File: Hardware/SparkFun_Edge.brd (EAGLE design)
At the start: 40 x 40 mm, 95 parts, among them J5 CORTEX_DEBUG, J7 CAMERA-HIMAX, U2 LIS2DH12, U3 1.8V, U5 ARTEMIS_MODULESMD, Y2 32.768kHz

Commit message: Rename files. Remove dependancy on Ambiq lbr. Remove ambiq.lbr.
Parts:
- C1, C10, C18, C20, C22, C9: device ambiq:0402-TIGHT -> SparkFun-Capacitors:0402-TIGHT
- C23: value 1.0uF -> 0.1uF; device ambiq:0402-TIGHT -> SparkFun-Capacitors:0402-TIGHT
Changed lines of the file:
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@@
 <?xml version="1.0" encoding="utf-8"?>
 <!DOCTYPE eagle SYSTEM "eagle.dtd">
-<eagle version="9.5.1">
+<eagle version="9.4.2">
 <drawing>
 <settings>
@@
 <attribute name="VALUE" x="26.0134" y="16.9958" size="0.6096" layer="27" font="vector" ratio="20" rot="R90" align="top-center"/>
 </element>
-<element name="C9" library="ambiq" package="0402-TIGHT" value="15pF" x="23" y="16" smashed="yes" rot="R270">
+<element name="C9" library="SparkFun-Capacitors" package="0402-TIGHT" value="15pF" x="23" y="16" smashed="yes" rot="R270">
 <attribute name="NAME" x="23.562" y="16" size="0.6096" layer="25" font="vector" ratio="20" rot="R270" align="bottom-center"/>
 <attribute name="PROD_ID" value="CAP-13063" x="23" y="16" size="1.778" layer="27" font="vector" ratio="15" rot="R270" display="off"/>
 <attribute name="VALUE" x="22.438" y="15.746" size="0.6096" layer="27" font="vector" ratio="20" rot="R270" align="top-center"/>
 </element>
-<element name="C10" library="ambiq" package="0402-TIGHT" value="15pF" x="23" y="18" smashed="yes" rot="R90">
+<element name="C10" library="SparkFun-Capacitors" package="0402-TIGHT" value="15pF" x="23" y="18" smashed="yes" rot="R90">
 <attribute name="NAME" x="22.438" y="18" size="0.6096" layer="25" font="vector" ratio="20" rot="R90" align="bottom-center"/>
 <attribute name="PROD_ID" value="CAP-13063" x="23" y="18" size="1.778" layer="27" font="vector" ratio="15" rot="R90" display="off"/>
@@
 <attribute name="VALUE" x="24.5902" y="10.9964" size="0.6096" layer="27" font="vector" ratio="20" rot="R90" align="top-center"/>
 </element>
-<element name="C20" library="ambiq" package="0402-TIGHT" value="0.1uF" x="22.5" y="11" smashed="yes" rot="R270">
+<element name="C20" library="SparkFun-Capacitors" package="0402-TIGHT" value="0.1uF" x="22.5" y="11" smashed="yes" rot="R270">
 <attribute name="NAME" x="23.062" y="11" size="0.6096" layer="25" font="vector" ratio="20" rot="R270" align="bottom-center"/>
 <attribute name="PROD_ID" value="CAP-12416" x="22.5" y="11" size="1.778" layer="27" font="vector" ratio="15" rot="R270" display="off"/>
@@
 <attribute name="VALUE" x="18.408" y="28.734" size="0.4064" layer="27"/>
 </element>
-<element name="C22" library="ambiq" package="0402-TIGHT" value="1.0uF" x="21" y="29" smashed="yes" rot="R270">
+<element name="C22" library="SparkFun-Capacitors" package="0402-TIGHT" value="1.0uF" x="21" y="29" smashed="yes" rot="R270">
 <attribute name="NAME" x="21.562" y="29" size="0.6096" layer="25" font="vector" ratio="20" rot="R270" align="bottom-center"/>
 <attribute name="PROD_ID" value="CAP-12417" x="21" y="29" size="1.778" layer="27" font="vector" ratio="15" rot="R270" display="off"/>
 <attribute name="VALUE" x="20.575" y="30.147" size="0.6096" layer="27" font="vector" ratio="20" rot="R270" align="top-center"/>
 </element>
-<element name="C23" library="ambiq" package="0402-TIGHT" value="1.0uF" x="19" y="31.5" smashed="yes">
+<element name="C23" library="SparkFun-Capacitors" package="0402-TIGHT" value="0.1uF" x="19" y="31.5" smashed="yes">
 <attribute name="NAME" x="19" y="32.062" size="0.6096" layer="25" font="vector" ratio="20" align="bottom-center"/>
-<attribute name="PROD_ID" value="CAP-12417" x="19" y="31.5" size="1.778" layer="27" font="vector" ratio="15" display="off"/>
-<attribute name="VALUE" x="19" y="30.938" size="0.6096" layer="27" font="vector" ratio="20" align="top-center"/>
+<attribute name="PROD_ID" value="CAP-12416" x="19" y="31.5" size="1.778" layer="27" font="vector" ratio="15" display="off"/>
+<attribute name="VALUE" value="0.1uF" x="19" y="30.938" size="0.6096" layer="27" font="vector" ratio="20" align="top-center"/>
 </element>
 <element name="D4" library="SparkFun-LED" package="LED-0603" value="BLUE" x="17" y="4" smashed="yes" rot="R270">
@@
 <attribute name="VALUE" x="11" y="20.762" size="0.6096" layer="27" font="vector" ratio="20" rot="R180" align="top-center"/>
 </element>
-<element name="C18" library="ambiq" package="0402-TIGHT" value="0.1uF" x="5.5" y="30" smashed="yes" rot="R90">
+<element name="C18" library="SparkFun-Capacitors" package="0402-TIGHT" value="0.1uF" x="5.5" y="30" smashed="yes" rot="R90">
 <attribute name="NAME" x="4.938" y="30" size="0.6096" layer="25" font="vector" ratio="20" rot="R90" align="bottom-center"/>
 <attribute name="PROD_ID" value="CAP-12416" x="5.5" y="30" size="1.778" layer="27" font="vector" ratio="15" rot="R90" display="off"/>
@@
 <attribute name="VALUE" x="0.1" y="11.6" size="0.6" layer="27" font="vector" rot="R270"/>
 </element>
-<element name="C1" library="ambiq" package="0402-TIGHT" value="0.1uF" x="5.5" y="10" smashed="yes" rot="R90">
+<element name="C1" library="SparkFun-Capacitors" package="0402-TIGHT" value="0.1uF" x="5.5" y="10" smashed="yes" rot="R90">
 <attribute name="NAME" x="4.938" y="10" size="0.6096" layer="25" font="vector" ratio="20" rot="R90" align="bottom-center"/>
 <attribute name="PROD_ID" value="CAP-12416" x="-0.5" y="6" size="1.778" layer="27" font="vector" ratio="15" rot="R90" display="off"/>

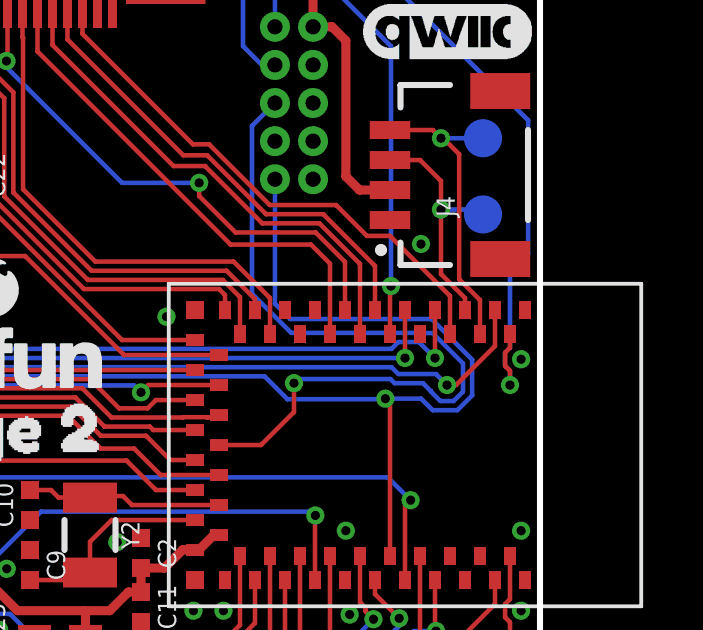
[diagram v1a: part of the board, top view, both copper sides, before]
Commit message: add gpio numbers to camera nets for ease of use
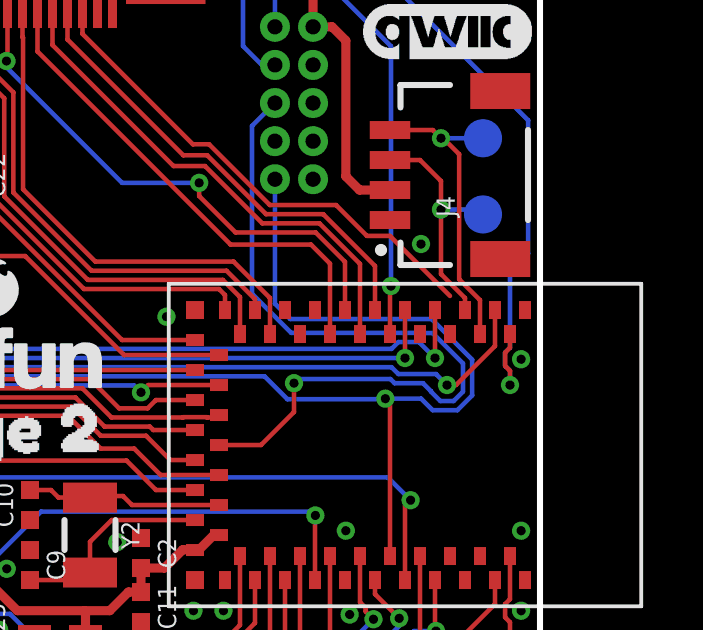
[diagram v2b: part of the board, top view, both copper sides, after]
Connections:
- net CAMERA_D0 renamed GPIO14/CAMERA_D0
- net CAMERA_D1 renamed GPIO11/CAMERA_D1
- net CAMERA_D2 renamed GPIO25/CAMERA_D2
- net CAMERA_D3 renamed GPIO34/CAMERA_D3
- net CAMERA_D4 renamed GPIO6/CAMERA_D4
- net CAMERA_D5 renamed GPIO5/CAMERA_D5
- net CAMERA_D6 renamed GPIO35/CAMERA_D6
- net CAMERA_D7 renamed GPIO28/CAMERA_D7
- net CAMERA_HSYNC renamed GPIO27/CAMERA_HSYNC
- net CAMERA_I2C_SCL renamed GPIO8/CAMERA_I2C_SCL
- net CAMERA_I2C_SDA renamed GPIO9/CAMERA_I2C_SDA
- net CAMERA_INT renamed GPIO23/CAMERA_INT
- net CAMERA_MCLK renamed GPIO26/CAMERA_MCLK
- net CAMERA_PCLK renamed GPIO7/CAMERA_PCLK
- net CAMERA_TRIG renamed GPIO13/CAMERA_TRIG
- net CAMERA_VSYNC renamed GPIO15/CAMERA_VSYNC
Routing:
- net GPIO9/CAMERA_I2C_SDA: track 18.0 -> 16.8 mm
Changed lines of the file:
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@@
 <?xml version="1.0" encoding="utf-8"?>
 <!DOCTYPE eagle SYSTEM "eagle.dtd">
-<eagle version="9.4.2">
+<eagle version="9.5.0">
 <drawing>
 <settings>
@@
 <setting verticaltext="up"/>
 </settings>
-<grid distance="0.05" unitdist="inch" unit="inch" style="lines" multiple="1" display="yes" altdistance="0.005" altunitdist="inch" altunit="inch"/>
+<grid distance="5" unitdist="mil" unit="mil" style="lines" multiple="1" display="yes" altdistance="1" altunitdist="mil" altunit="mil"/>
 <layers>
 <layer number="1" name="Top" color="4" fill="1" visible="yes" active="yes"/>
@@
 <wire x1="6.5" y1="23.81" x2="4.79" y2="23.81" width="0.1524" layer="1"/>
 </signal>
-<signal name="CAMERA_D3">
+<signal name="GPIO34/CAMERA_D3">
 <contactref element="J7" pad="5"/>
 <wire x1="26.86865625" y1="20.3092" x2="25.35974375" y2="20.3092" width="0.1524" layer="1"/>
@@
 <wire x1="27.67785625" y1="19.5" x2="26.86865625" y2="20.3092" width="0.1524" layer="1"/>
 </signal>
-<signal name="CAMERA_D1">
+<signal name="GPIO11/CAMERA_D1">
 <contactref element="J7" pad="3"/>
 <wire x1="15.25" y1="33.3" x2="15.25" y2="34.6" width="0.1524" layer="1"/>
@@
 <wire x1="27.355" y1="19" x2="26.474" y2="19.881" width="0.1524" layer="1"/>
 </signal>
-<signal name="CAMERA_D2">
+<signal name="GPIO25/CAMERA_D2">
 <contactref element="J7" pad="9"/>
 <contactref element="U5" pad="~D25"/>
@@
 <wire x1="17.5" y1="32" x2="18.25" y2="32.75" width="0.1524" layer="1"/>
 </signal>
-<signal name="CAMERA_VSYNC">
+<signal name="GPIO15/CAMERA_VSYNC">
 <contactref element="J7" pad="6"/>
 <wire x1="25.486" y1="20.614" x2="24.5144" y2="21.5856" width="0.1524" layer="1"/>
@@
 <wire x1="26.9949125" y1="20.614" x2="25.486" y2="20.614" width="0.1524" layer="1"/>
 </signal>
-<signal name="CAMERA_INT">
+<signal name="GPIO23/CAMERA_INT">
 <contactref element="J7" pad="18"/>
 <wire x1="22.76894375" y1="33.57894375" x2="22.75" y2="33.5978875" width="0.1524" layer="1"/>
@@
 <wire x1="23.0426" y1="13.6604" x2="33.91503125" y2="13.6604" width="0.1524" layer="16"/>
 </signal>
-<signal name="CAMERA_D4">
+<signal name="GPIO6/CAMERA_D4">
 <contactref element="J7" pad="12"/>
 <contactref element="U5" pad="~D6"/>
@@
 <wire x1="21.5286" y1="31.3092875" x2="19.75" y2="33.0878875" width="0.1524" layer="1"/>
 </signal>
-<signal name="CAMERA_I2C_SDA">
-<contactref element="J7" pad="22"/>
-<contactref element="U5" pad="D9"/>
-<wire x1="37" y1="24.96894375" x2="37" y2="23.7" width="0.1524" layer="1"/>
-<wire x1="24.75" y1="34.6" x2="24.75" y2="33.704" width="0.1524" layer="1"/>
-<wire x1="24.75" y1="33.704" x2="28.429" y2="30.025" width="0.1524" layer="1"/>
-<wire x1="34.2303125" y1="26.9714" x2="34.99754375" y2="26.9714" width="0.1524" layer="1"/>
-<wire x1="33.2017125" y1="28" x2="34.2303125" y2="26.9714" width="0.1524" layer="1"/>
-<wire x1="34.99754375" y1="26.9714" x2="37" y2="24.96894375" width="0.1524" layer="1"/>
-<wire x1="30.9946" y1="28" x2="33.2017125" y2="28" width="0.1524" layer="1"/>
-<wire x1="28.9696" y1="30.025" x2="28.429" y2="30.025" width="0.1524" layer="1"/>
-<wire x1="30.9946" y1="28" x2="28.9696" y2="30.025" width="0.1524" layer="1"/>
-</signal>
-<signal name="CAMERA_I2C_SCL">
+<signal name="GPIO8/CAMERA_I2C_SCL">
 <contactref element="J7" pad="21"/>
 <contactref element="U5" pad="D8"/>
@@
 <wire x1="19" y1="6.15" x2="19" y2="4.877" width="0.1524" layer="1"/>
 </signal>
-<signal name="CAMERA_D0">
+<signal name="GPIO14/CAMERA_D0">
 <contactref element="J7" pad="14"/>
 <wire x1="20.75" y1="34.6" x2="20.75" y2="32.95" width="0.1524" layer="1"/>
@@
 <wire x1="30" y1="24.93105625" x2="29.42625625" y2="25.5048" width="0.1524" layer="1"/>
 </signal>
-<signal name="CAMERA_TRIG">
+<signal name="GPIO13/CAMERA_TRIG">
 <contactref element="J7" pad="7"/>
 <wire x1="17.25" y1="34.6" x2="17.25" y2="32.6121125" width="0.1524" layer="1"/>
@@
 <wire x1="24.75" y1="15.5" x2="23" y2="15.5" width="0.1524" layer="1"/>
 </signal>
-<signal name="CAMERA_HSYNC">
+<signal name="GPIO27/CAMERA_HSYNC">
 <contactref element="J7" pad="16"/>
 <wire x1="21.75" y1="34.6" x2="21.75" y2="33.08774375" width="0.1524" layer="1"/>
@@
 <wire x1="25.0525125" y1="25.8096" x2="22.4452" y2="28.4169125" width="0.1524" layer="1"/>
 </signal>
-<signal name="CAMERA_D7">
+<signal name="GPIO28/CAMERA_D7">
 <contactref element="J7" pad="13"/>
 <wire x1="21.8356" y1="28.1644" x2="21.8356" y2="31.43334375" width="0.1524" layer="1"/>
@@
 <wire x1="24.8" y1="25.2" x2="21.8356" y2="28.1644" width="0.1524" layer="1"/>
 </signal>
-<signal name="CAMERA_MCLK">
+<signal name="GPIO26/CAMERA_MCLK">
 <contactref element="J7" pad="8"/>
 <contactref element="U5" pad="~D26"/>
@@
 <wire x1="17.1952" y1="32.12625625" x2="17.75" y2="32.68105625" width="0.1524" layer="1"/>
 </signal>
-<signal name="CAMERA_D6">
+<signal name="GPIO35/CAMERA_D6">
 <contactref element="J7" pad="19"/>
 <contactref element="U5" pad="~AD35"/>
@@
 <wire x1="23.25" y1="33.1198" x2="23.25" y2="34.6" width="0.1524" layer="1"/>
 </signal>
-<signal name="CAMERA_D5">
+<signal name="GPIO5/CAMERA_D5">
 <contactref element="J7" pad="20"/>
 <contactref element="U5" pad="~D5"/>
@@
 <wire x1="32.6474875" y1="27.3904" x2="34" y2="26.0378875" width="0.1524" layer="1"/>
 </signal>
-<signal name="CAMERA_PCLK">
+<signal name="GPIO7/CAMERA_PCLK">
 <contactref element="J7" pad="17"/>
 <contactref element="U5" pad="D7"/>
@@
 <wire x1="10.16" y1="8.382" x2="10.16" y2="3.048" width="0.3048" layer="1"/>
 </signal>
+<signal name="GPIO9/CAMERA_I2C_SDA">
+<contactref element="U5" pad="D9"/>
+<contactref element="J7" pad="22"/>
+<wire x1="24.75" y1="34.6" x2="24.75" y2="33.704" width="0.1524" layer="1"/>
+<wire x1="24.75" y1="33.704" x2="28.429" y2="30.025" width="0.1524" layer="1"/>
+<wire x1="34.2303125" y1="26.9714" x2="34.99754375" y2="26.9714" width="0.1524" layer="1"/>
+<wire x1="33.2017125" y1="28" x2="34.2303125" y2="26.9714" width="0.1524" layer="1"/>
+<wire x1="34.99754375" y1="26.9714" x2="37" y2="24.96894375" width="0.1524" layer="1"/>
+<wire x1="30.9946" y1="28" x2="33.2017125" y2="28" width="0.1524" layer="1"/>
+<wire x1="28.9696" y1="30.025" x2="28.429" y2="30.025" width="0.1524" layer="1"/>
+<wire x1="30.9946" y1="28" x2="28.9696" y2="30.025" width="0.1524" layer="1"/>
+<wire x1="37" y1="24.96894375" x2="37" y2="23.7" width="0" layer="19" extent="1-1"/>
+</signal>
 </signals>

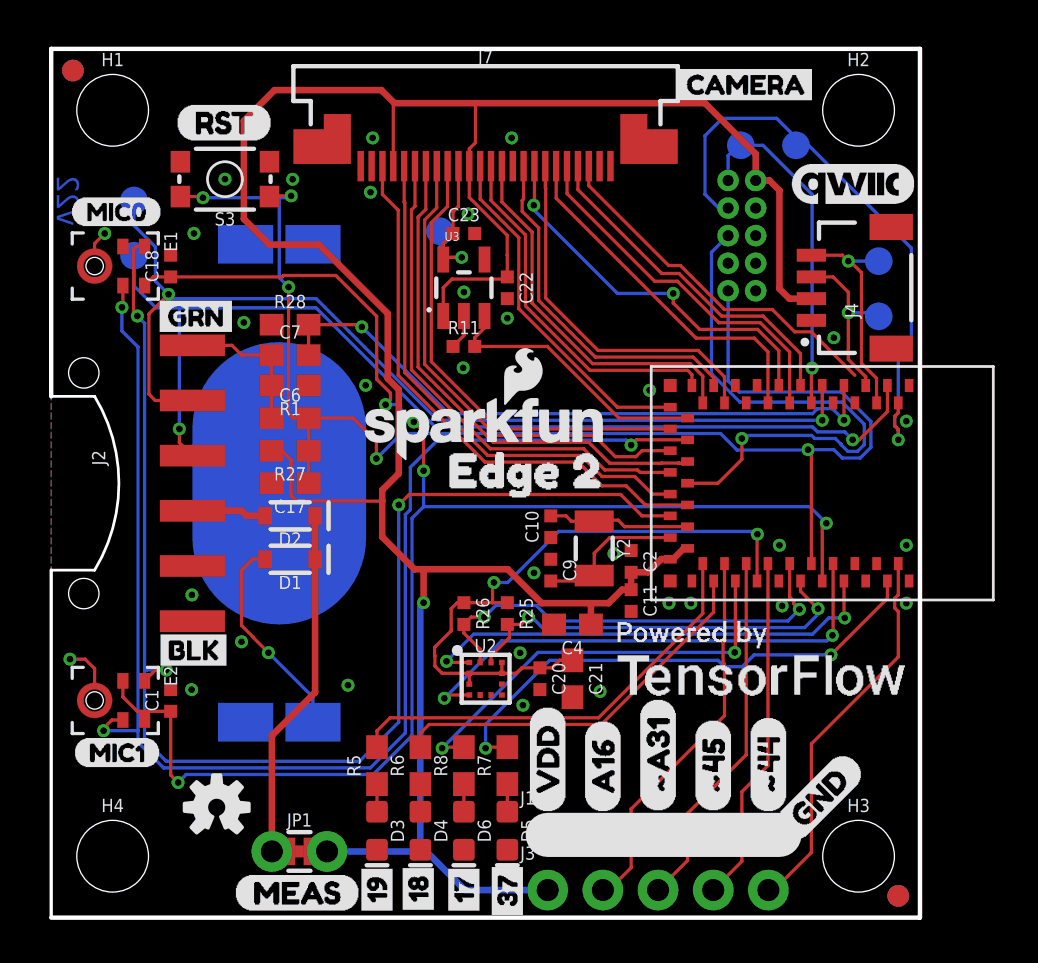
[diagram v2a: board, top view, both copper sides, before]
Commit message: re-assign camera pins for fast gpio compatibility
Camera Pin : FAST GPIO Bit : Apollo3 Pad
D0 : D0 : 24
D1 : D1 : 33
D2 : D2 : 10
D3 : D3 : 11
D4 : D4 : 28
D5 : D5 : 5
D6 : D6 : 14
D7 : D7 : 23
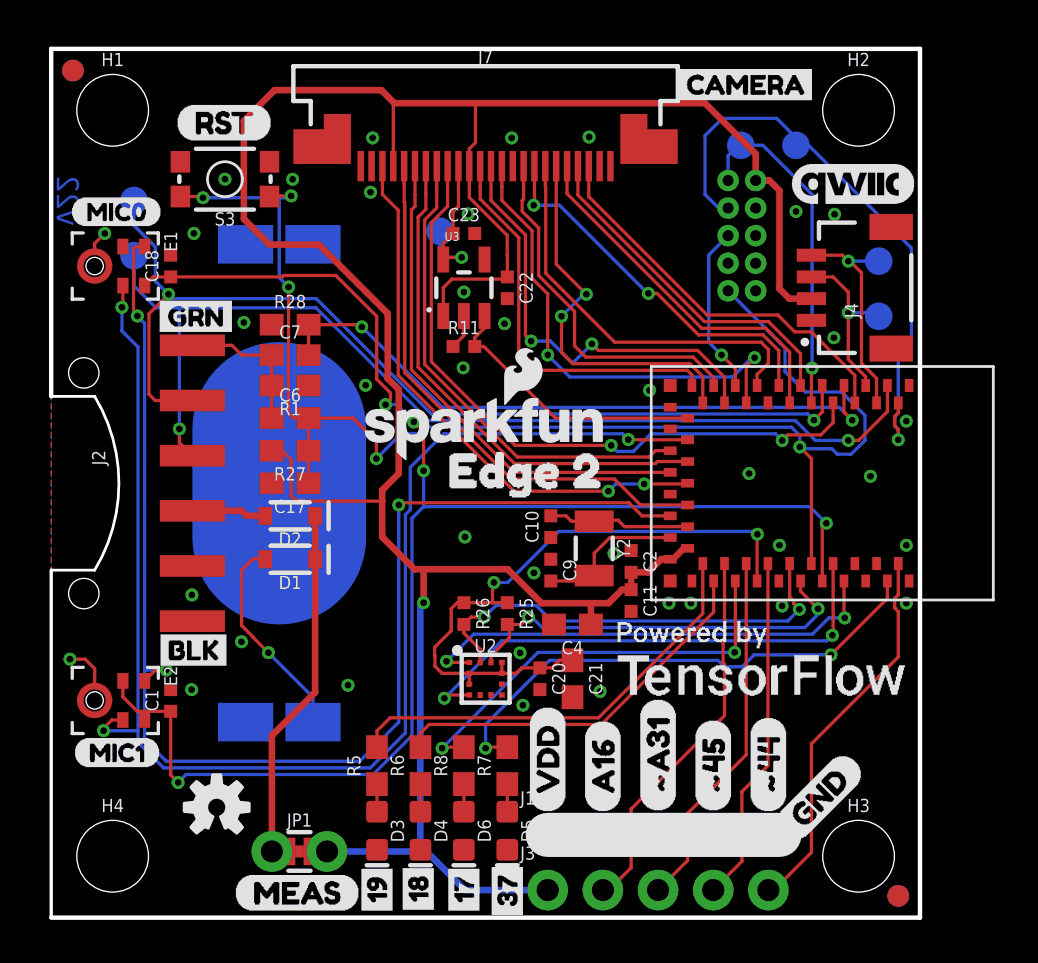
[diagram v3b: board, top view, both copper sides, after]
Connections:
- removed net GPIO11/CAMERA_D1: J7.3, U5.~AD11
- removed net GPIO23/CAMERA_INT: J7.18, U5.~D23
- removed net GPIO25/CAMERA_D2: J7.9, U5.~D25
- removed net GPIO28/CAMERA_D7: J7.13, U5.~D28
- removed net GPIO34/CAMERA_D3: J7.5, U5.AD34
- removed net GPIO35/CAMERA_D6: J7.19, U5.~AD35
- removed net GPIO6/CAMERA_D4: J7.12, U5.~D6
- removed net ~AD33/SWO: J5.6, U5.~AD33/SWO
- new net GPIO10/CAMERA_D2: J7.9, U5.D10
- new net GPIO11/CAMERA_D3: J7.5, U5.~AD11
- new net GPIO23/CAMERA_D7: J7.13, U5.~D23
- new net GPIO24/CAMERA_D0: J7.14, U5.~D24
- new net GPIO28/CAMERA_D4: J7.12, U5.~D28
- new net GPIO33/CAMERA_D1: J7.3, U5.~AD33/SWO
- new net GPIO4/CAMERA_INT: J7.18, U5.~D4
- new net ~D22/SWO: J5.6, U5.~D22
- net GPIO14/CAMERA_D0: now also J7.19; no longer J7.14
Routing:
- net GPIO10/CAMERA_D2: track 0.00 -> 31.2 mm, vias 0 -> 2
- net GPIO11/CAMERA_D1: track 25.7 -> 0.00 mm
- net ~AD33/SWO: track 25.7 -> 0.00 mm, vias 1 -> 0
- net GPIO33/CAMERA_D1: track 0.00 -> 25.6 mm, vias 0 -> 2
- net GPIO11/CAMERA_D3: track 0.00 -> 25.1 mm
- net GPIO34/CAMERA_D3: track 24.1 -> 0.00 mm
- net GPIO24/CAMERA_D0: track 0.00 -> 22.1 mm, vias 0 -> 2
- net GPIO25/CAMERA_D2: track 21.6 -> 0.00 mm
- net GPIO23/CAMERA_D7: track 0.00 -> 20.3 mm, vias 0 -> 2
- net GPIO4/CAMERA_INT: track 0.00 -> 18.5 mm
- net GPIO28/CAMERA_D4: track 0.00 -> 18.1 mm
- net GPIO23/CAMERA_INT: track 17.0 -> 0.00 mm
- net GPIO28/CAMERA_D7: track 16.6 -> 0.00 mm
- net GPIO35/CAMERA_D6: track 16.5 -> 0.00 mm
- net GPIO6/CAMERA_D4: track 16.1 -> 0.00 mm
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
